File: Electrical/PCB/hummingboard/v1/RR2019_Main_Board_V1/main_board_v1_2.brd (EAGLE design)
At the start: 100 x 75 mm, 147 parts, among them CN1 MIRCO_B, IC1 OR_SC70-5, J10 I2C_5V_4, J11 SERVO_LEFT, J12 SERVO_RIGHT, J13 ESC, J14 5V_INPUT, J15 QUAD_ENCODER_2, J16 7.2V_INPUT, J17 I2C_5V_FXIO_1, J18 I2C_5V_FXIO_2, J19 JETSON_TRIGGER, J2 REAR_ENCODER, J20 QUAD_ENCODER_1, J21 BLDC_HALL, J22 SPI_FXIO_1, J3 FRONT_ENCODER, J4 I2C_1V8_1, J5 SPI_2, J6 WIRELESS_MODULE, J7 UART_0, J8 UART_2, J9 STEERING_ANGLE, Q1 BSS138, Q3 DMP2066LSN, Q4 BSS138, Q5 BSS138, Q6 BSS138, Q7 BSS138, Q8 BSS138, U3 ICM-20948, U4 PCA9306

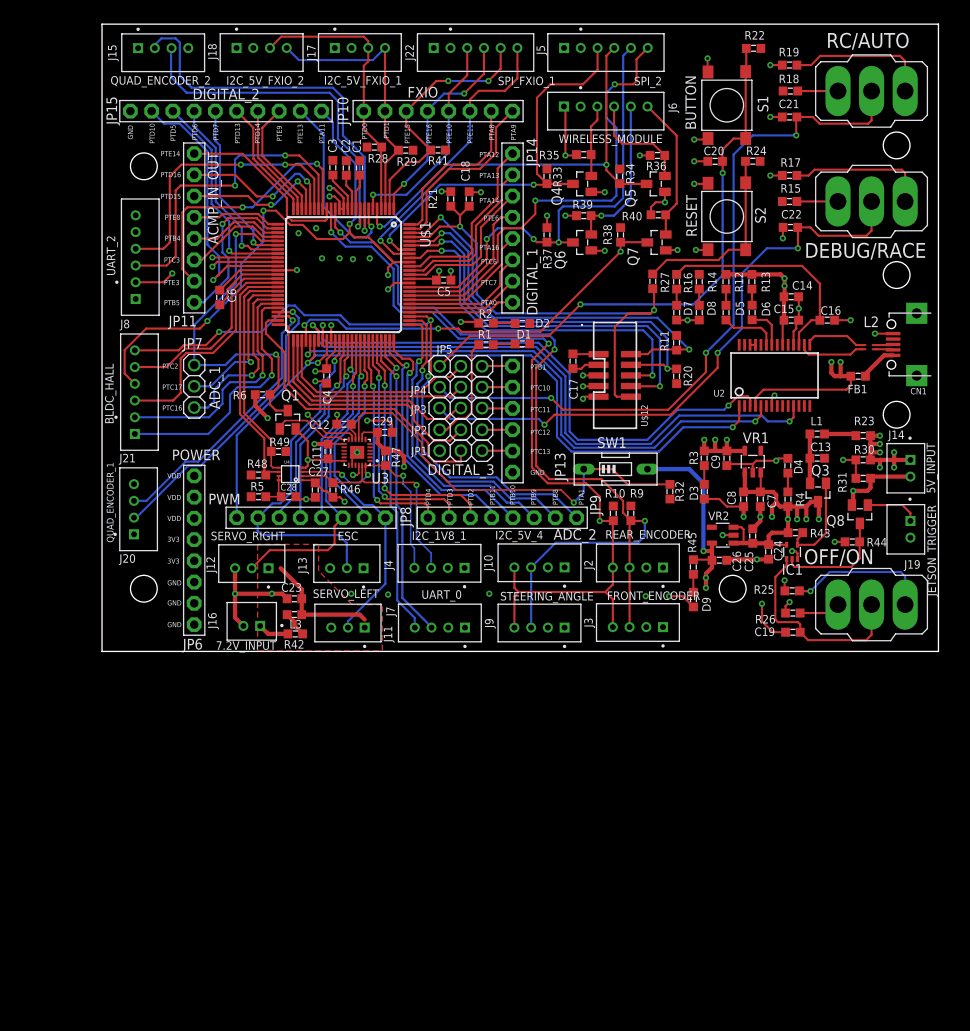
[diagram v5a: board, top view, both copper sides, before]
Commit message: change 2 switch to DIP and toggle smaller
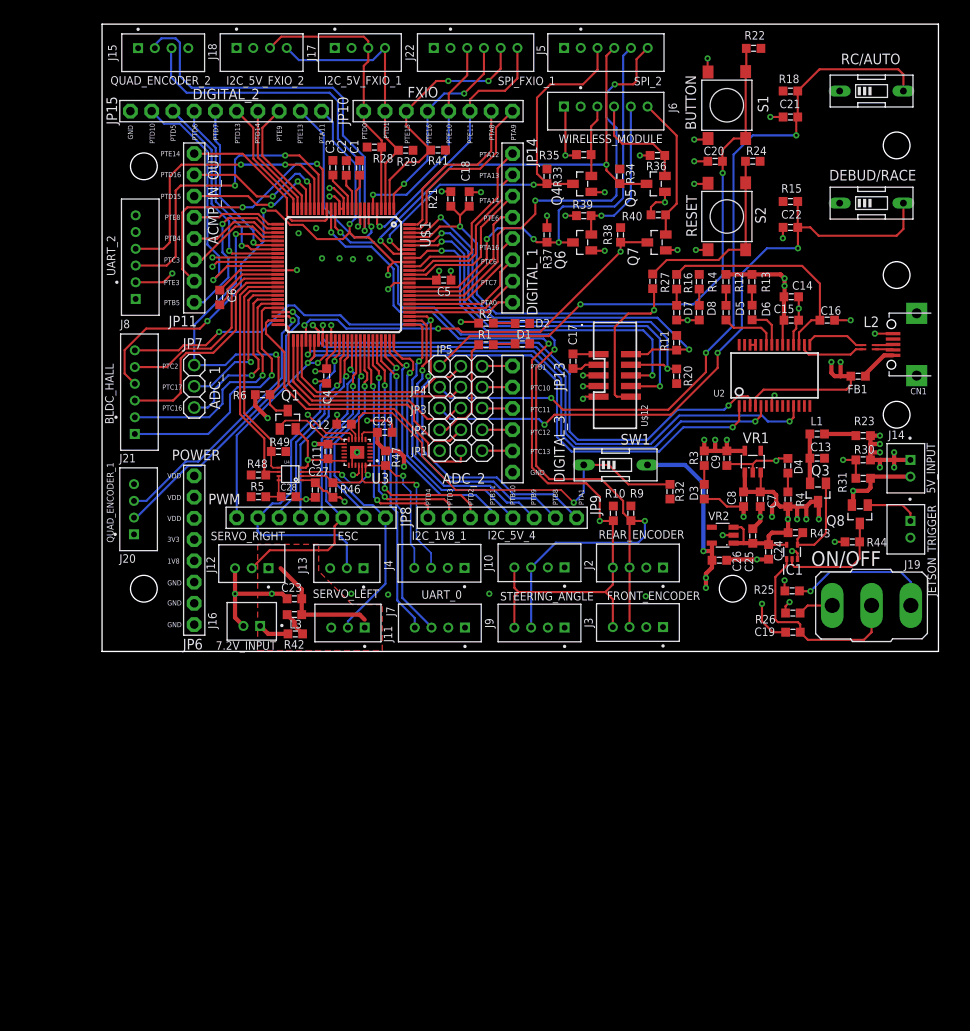
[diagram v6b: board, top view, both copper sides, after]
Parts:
- removed D9: LED_GREEN, RobotRacing2019_Master:0603SMT
- removed DEBUG/RACE, OFF/ON: (no value), switch:320-916
- removed R17, R19: 10K, RobotRacing2019_Master:0603SMT
- removed R45: 150, RobotRacing2019_Master:0603SMT
- added DEBUD/RACE: (no value), special:EDG-01
- added S3: ON/OFF, RobotRacing2019_Master:M9040P
- R1, R14, R2: value (none) -> 300
- R12, R13: value 1k -> 300
- R15, R18: value 10K -> 100k
- R16: value (none) -> 120
- R3: value 150 -> 120
- R4: value 150 -> 300
- RC/AUTO: device switch:320-916 -> special:EDG-01
- moved SW1 0.50 mm to (61.4, 22.3)
- moved C21 0.10 mm to (82.3, 63.9)
- moved R15 0.10 mm to (82.3, 53.8)
- turned RC/AUTO to 270 degrees
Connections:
- removed net N$28: DEBUG/RACE.3, R17.2
- removed net N$32: R18.1, RC/AUTO.1
- removed net N$33: R19.2, RC/AUTO.3
- removed net N$4: C22.1, DEBUG/RACE.2, JP3.1
- removed net N$42: D9.1, R45.1
- net +1.8V: now also JP6.5; no longer R45.2
- net +3V3: no longer JP6.5
- net GND: now also DEBUD/RACE.1, RC/AUTO.1; no longer D9.2, R17.1, R19.1
- net N$26: now also C22.1, DEBUD/RACE.2, JP3.1; no longer DEBUG/RACE.1
- net N$31: now also R18.1
- net N$45: now also S3.3; no longer OFF/ON.3
- net N$46: now also S3.1; no longer OFF/ON.1
- net POWER_SHUT_DOWN: now also S3.2; no longer OFF/ON.2
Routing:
- net N$26: track 4.91 -> 79.4 mm, vias 0 -> 3
- net N$4: track 72.8 -> 0.00 mm, vias 3 -> 0
- net N$33: track 17.2 -> 0.00 mm
- net N$28: track 16.8 -> 0.00 mm
- net N$31: track 85.8 -> 92.0 mm
- net GND: track 153.9 -> 147.7 mm, vias 48 -> 45
- net N$32: track 4.81 -> 0.00 mm
- net N$42: track 2.15 -> 0.00 mm
- net +1.8V: track 48.2 -> 46.3 mm
- net N$45: track 4.94 -> 4.21 mm
- net N$22: track 49.5 -> 50.2 mm
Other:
- board text added: "1V8"

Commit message: layout complete v.1
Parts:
- added JP12: POWER2, adafruit:1X03
- moved R49 2.40 mm to (18.7, 23.9), turned to 180 degrees
- moved R34 1.80 mm to (62.0, 55.0), turned to 270 degrees
- moved RC/AUTO 1.70 mm to (92.0, 65.3)
- moved R33 1.70 mm to (53.2, 55.1), turned to 270 degrees
- moved C1 1.00 mm to (31.8, 57.8)
- moved C2 0.81 mm to (30.0, 57.9)
- moved R3 0.60 mm to (71.4, 23.1)
- moved C24 0.20 mm to (79.9, 11.9)
- moved R28 0.20 mm to (32.6, 60.5)
- moved R31 0.20 mm to (91.0, 20.5)
- moved C17 0.20 mm to (56.3, 34.9)
- moved C3 0.14 mm to (27.7, 57.9)
- moved C25 0.10 mm to (77.7, 13.8)
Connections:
- net +1.8V: now also JP6.4; no longer JP6.5
- net +3V3: now also JP12.1, JP12.2; no longer JP6.4
- net GND: now also JP12.3, JP6.5
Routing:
- net +VDD: track 79.9 -> 158.4 mm, vias 11 -> 35
- net +3V3: track 27.5 -> 72.2 mm, vias 10 -> 11
- net GND: track 147.7 -> 178.9 mm, vias 45 -> 74
- net +VUSB: track 64.7 -> 38.1 mm, vias 4 -> 5
- net +5V: track 42.9 -> 20.0 mm
- net SPI0_PCS0: track 48.9 -> 53.3 mm
- net +1.8V: track 46.3 -> 48.4 mm, vias 8 -> 9
- net I2C0_SCL: track 106.1 -> 104.1 mm, vias 3 -> 4
- net PWT_IN1_/_FXIO_D5: track 32.6 -> 33.6 mm
- net N$31: track 92.0 -> 91.2 mm
- net FTM2_CH6_/_FXIO_D2_/_TRGMUX_OUT6: track 31.6 -> 32.2 mm
- net FXIO_D0_/_ADC2_SE0: track 33.7 -> 34.3 mm
- net SPI0_MOSI: track 55.6 -> 56.2 mm
- net I2C1__SCL: track 30.3 -> 29.7 mm, vias 0 -> 2
- net ADC0_SE15_/_PTC17: track 105.1 -> 105.3 mm, vias 2 -> 3
- added copper zone on layer 15, net +VDD
- added copper zone on layer 16, net +VDD
- added copper zone on layer 16, net +VUSB
- added copper zone on layer 1, net GND
- added copper zone on layer 16, net GND
- removed copper zone on layer 15, net +VUSB
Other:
- board text added: "+"

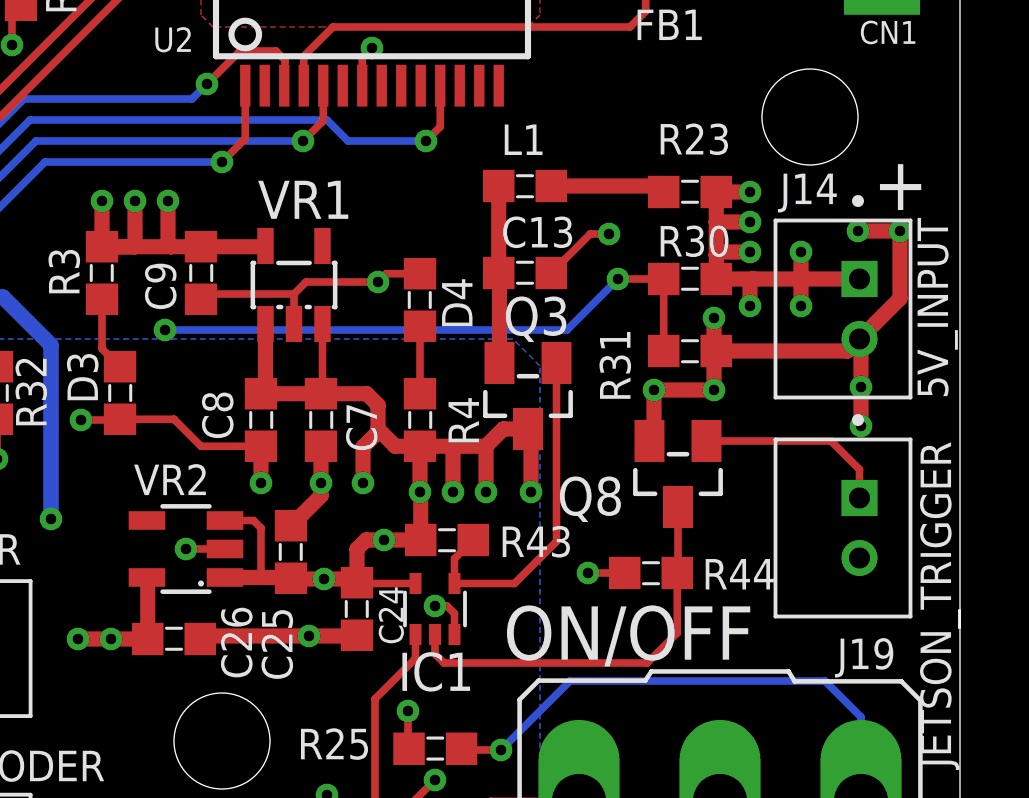
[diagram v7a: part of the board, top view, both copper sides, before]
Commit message: layout and power planed modified, complete v2
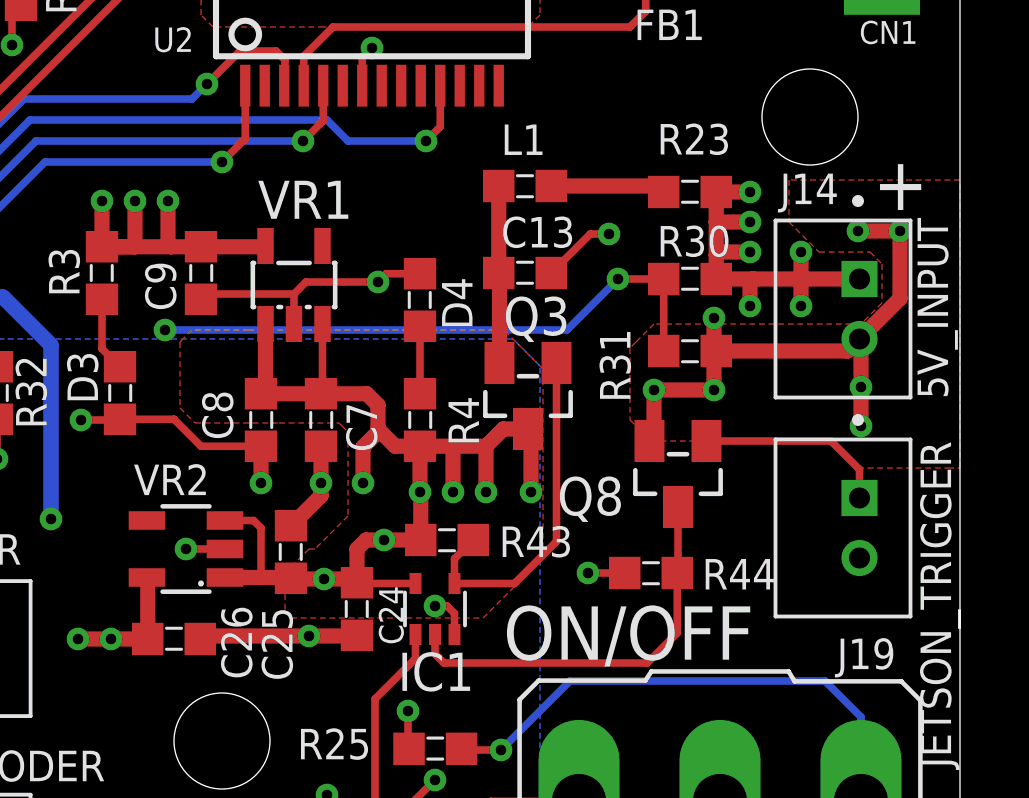
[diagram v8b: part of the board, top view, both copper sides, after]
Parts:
- moved U$44 0.10 mm to (28.3, 44.1)
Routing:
- net +VDD: track 158.4 -> 153.9 mm
- added copper zone on layer 1, net +VDD
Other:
- board text added: "HUMMINGBOT"
- board text added: "UW ROBOTICS 2019"
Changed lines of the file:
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@@
 <text x="89.7" y="72.8" size="0.6096" layer="21" rot="R90">3V3</text>
 <text x="92.3" y="72.8" size="0.6096" layer="21" rot="R90">3V3</text>
+<text x="60.8" y="11.3" size="1.778" layer="22" rot="MR0">HUMMINGBOT</text>
+<text x="43.2" y="11.4" size="1.778" layer="22" rot="MR0">UW ROBOTICS 2019</text>
 </plain>
 <attributes>
@@
 <attribute name="NAME" x="25.1" y="1.35" size="1.016" layer="25" rot="R180"/>
 </element>
-<element name="U$44" library="RobotRacing2019_Master" package="TEAM_LOGO" value="TEAM_LOGO" x="28.3" y="44" smashed="yes" rot="MR0"/>
 <element name="J19" library="RobotRacing2019_Master" package="JST_B2B-PH-K-S(LF)(SN)" value="JETSON_TRIGGER" x="96.1" y="14.6" smashed="yes" rot="R90">
 <attribute name="NAME" x="95.89608125" y="9.89518125" size="1.01753125" layer="25"/>
@@
 <attribute name="VALUE" x="86.19" y="66.725" size="1.27" layer="21" rot="R90"/>
 </element>
+<element name="U$44" library="RobotRacing2019_Master" package="TEAM_LOGO" value="TEAM_LOGO" x="28.3" y="44.1" smashed="yes" rot="MR0"/>
 </elements>
 <signals>
@@
 <vertex x="75.1" y="35.7"/>
 </polygon>
+<polygon width="0.254" layer="1">
+<vertex x="89" y="19.6"/>
+<vertex x="89" y="18.2"/>
+<vertex x="89.7" y="17.5"/>
+<vertex x="94.1" y="17.5"/>
+<vertex x="95.7" y="17.5"/>
+<vertex x="96.6" y="16.6"/>
+<vertex x="99.6" y="16.6"/>
+<vertex x="100" y="16.6"/>
+<vertex x="100" y="26.2"/>
+<vertex x="94.3" y="26.2"/>
+<vertex x="94.3" y="24.8"/>
+<vertex x="95.3" y="23.8"/>
+<vertex x="97" y="23.8"/>
+<vertex x="97.4" y="23.4"/>
+<vertex x="97.4" y="22.1"/>
+<vertex x="96.7" y="21.4"/>
+<vertex x="92" y="21.4"/>
+<vertex x="89.8" y="21.4"/>
+<vertex x="89.2" y="20.8"/>
+<vertex x="89" y="20.6"/>
+<vertex x="89" y="19.7"/>
+</polygon>
 </signal>
 <signal name="+VDD">
@@
 <wire x1="78.7" y1="19.075" x2="78.75" y2="19.125" width="0.254" layer="1"/>
 <via x="83.1" y="15.8" extent="1-16" drill="0.35"/>
-<wire x1="76.675" y1="19.1" x2="76.7" y2="19.075" width="0.508" layer="1"/>
 <via x="85.7" y="15.8" extent="1-16" drill="0.35"/>
 <via x="84.2" y="15.8" extent="1-16" drill="0.35"/>
@@
 <wire x1="59.36" y1="35.54" x2="56.535" y2="35.54" width="0.254" layer="1"/>
 <wire x1="56.535" y1="35.54" x2="56.3" y2="35.775" width="0.254" layer="1"/>
-<wire x1="79.9" y1="12.775" x2="79.71980625" y2="13.15" width="0.254" layer="1"/>
 <via x="80.1" y="16.1" extent="1-16" drill="0.35"/>
-<wire x1="81.85" y1="14.025003125" x2="82.025" y2="14.2" width="0.254" layer="1"/>
 <wire x1="88.825" y1="13.1" x2="87.6" y2="13.1" width="0.254" layer="1"/>
 <via x="87.6" y="13.1" extent="1-16" drill="0.35"/>
@@
 <wire x1="78.775" y1="72.1" x2="80.2" y2="72.1" width="0.254" layer="1"/>
 <via x="80.2" y="72.1" extent="1-16" drill="0.35"/>
-<wire x1="77.85" y1="12.775" x2="77.7" y2="12.925" width="0.508" layer="1"/>
 <via x="80.8" y="14.2" extent="1-16" drill="0.35"/>
 <wire x1="80.8" y1="14.2" x2="82.025" y2="14.2" width="0.508" layer="1"/>
@@
 <wire x1="15.3" y1="73.5" x2="16.08" y2="72.72" width="0.508" layer="15"/>
 <wire x1="16.08" y1="72.72" x2="16.08" y2="72.15" width="0.508" layer="15"/>
-<wire x1="82.5" y1="6.2" x2="82.5" y2="9.8" width="0.508" layer="15"/>
 <polygon width="0.254" layer="16">
 <vertex x="52" y="13.1"/>
@@
 <wire x1="32.7" y1="56" x2="31.8" y2="56.9" width="0.508" layer="1"/>
 <wire x1="31.8" y1="56.9" x2="31.8" y2="56.935" width="0.508" layer="1"/>
+<polygon width="0.254" layer="1">
+<vertex x="76.3" y="21.2"/>
+<vertex x="74.4" y="21.2"/>
+<vertex x="74.1" y="20.9"/>
+<vertex x="74" y="20.8"/>
+<vertex x="74" y="18.9"/>
+<vertex x="74" y="18.6"/>
+<vertex x="74.5" y="18.1"/>
+<vertex x="77.3" y="18.1"/>
+<vertex x="79.3" y="18.1"/>
+<vertex x="79.4" y="18"/>
+<vertex x="79.6" y="17.8"/>
+<vertex x="79.6" y="15"/>
+<vertex x="78.5" y="13.9"/>
+<vertex x="78.3" y="13.9"/>
+<vertex x="77.5" y="13.1"/>
+<vertex x="77.5" y="12.4"/>
+<vertex x="77.5" y="11.8"/>
+<vertex x="77.7" y="11.6"/>
+<vertex x="84.1" y="11.6"/>
+<vertex x="86.1" y="13.6"/>
+<vertex x="86.1" y="19.9"/>
+<vertex x="84.8" y="21.2"/>
+</polygon>
 </signal>
 <signal name="N$3">
@@
 <mfgpreviewcolor name="substratecolor" color="0xFF786E46"/>
 </mfgpreviewcolors>
+<errors>
+</errors>
 </board>
 </drawing>
